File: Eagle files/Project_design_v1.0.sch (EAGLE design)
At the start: 4 parts

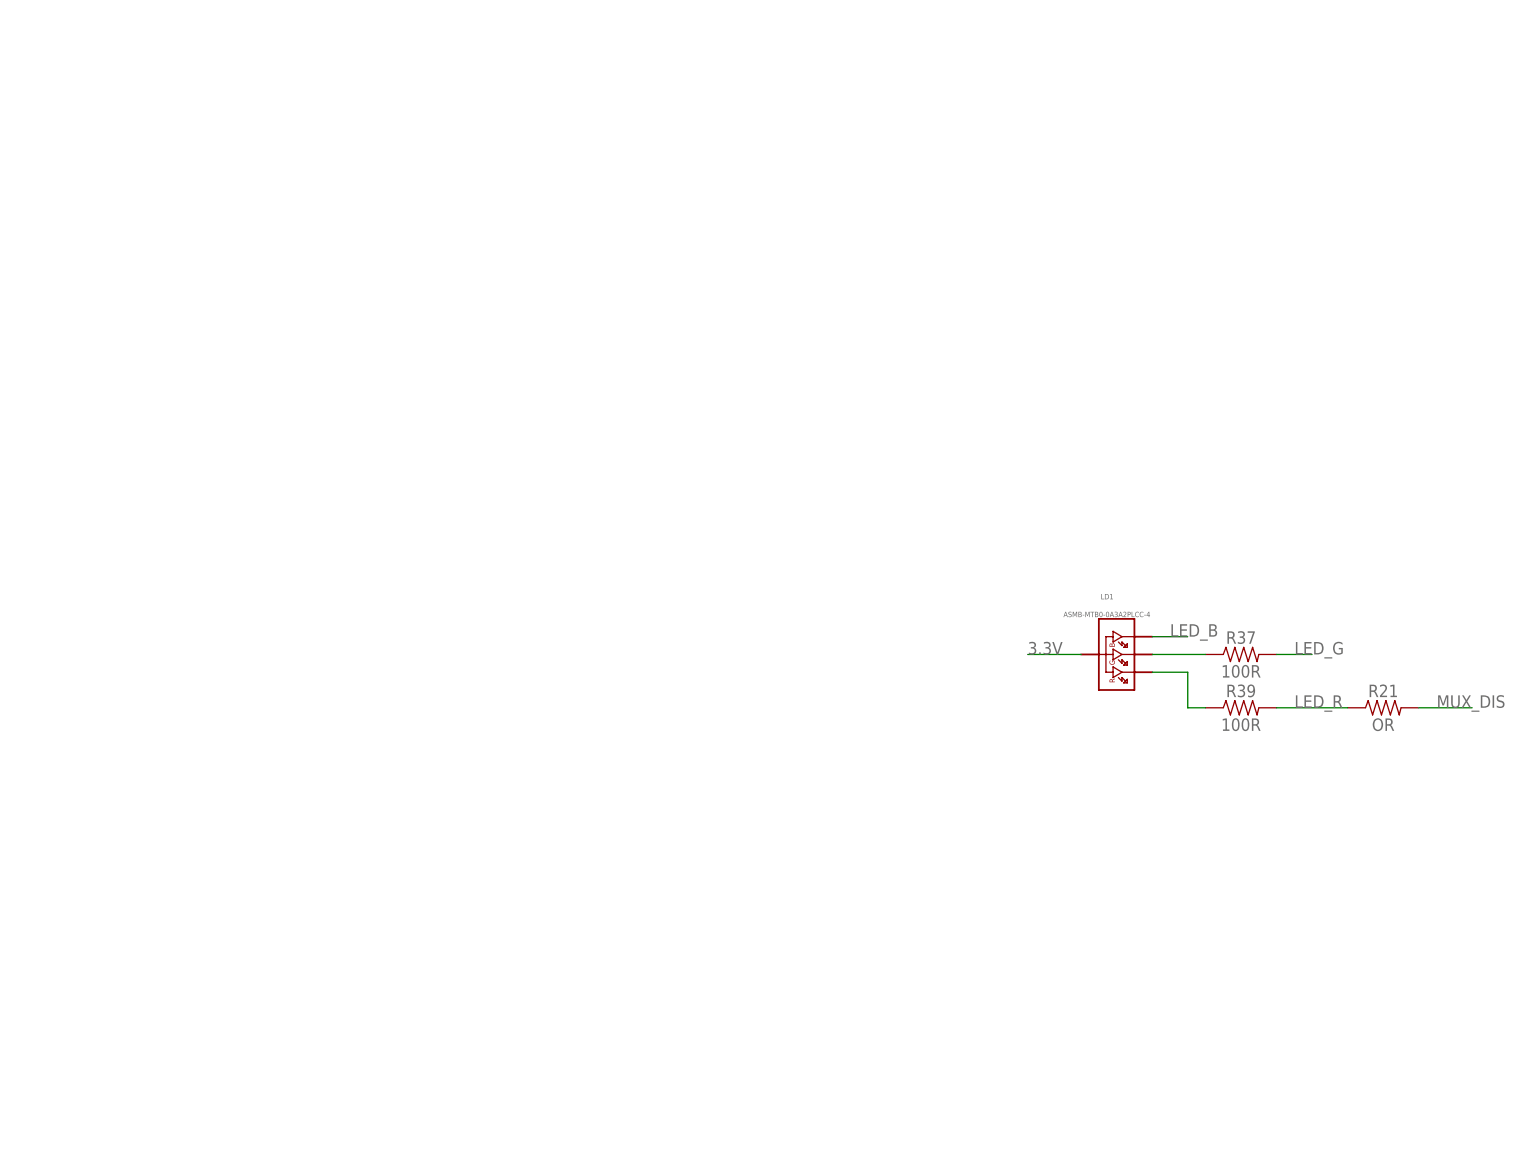
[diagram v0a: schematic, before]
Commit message: schematic des temperature, soil moisture, led, brightness sensor
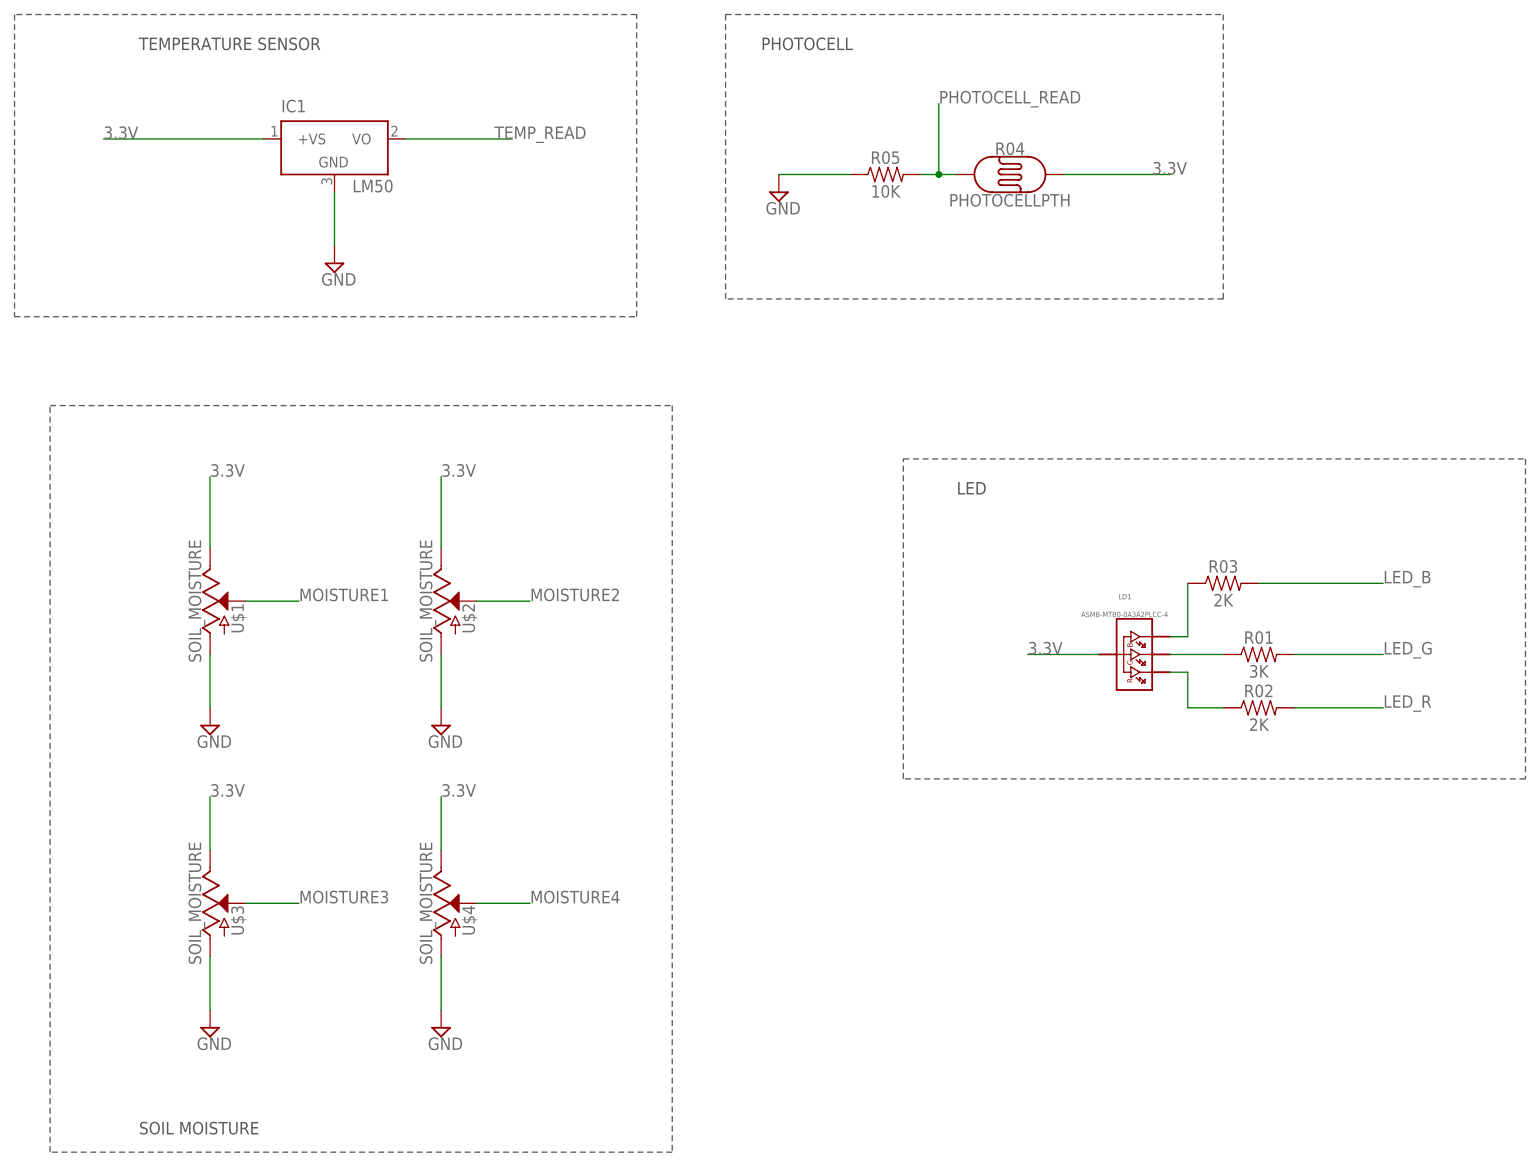
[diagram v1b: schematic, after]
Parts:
- removed R21: OR, custom_part:0603RESIST
- removed R37, R39: 100R, custom_part:0603RESIST
- added IC1: LM50, linear:LM50
- added R01: 3K, custom_part:0603RESIST
- added R02, R03: 2K, custom_part:0603RESIST
- added R04: PHOTOCELLPTH, SparkFun-Sensors:PHOTOCELLPTH
- added R05: 10K, custom_part:0603RESIST
- added U$1, U$2, U$3, U$4: SOIL_MOISTURE, potentiometer:SOIL_MOISTURE
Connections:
- removed net MUX_DIS: R21.2
- new net GND: R05.1, U$1.GND, U$2.GND, U$3.GND, U$4.GND
- new net MOISTURE1: U$1.VOUT
- new net MOISTURE2: U$2.VOUT
- new net MOISTURE3: U$3.VOUT
- new net MOISTURE4: U$4.VOUT
- new net N$1: LD1.2, R03.1
- new net N$4: IC1.GND
- new net PHOTOCELL_READ: R04.P$1, R05.2
- new net TEMP_READ: IC1.VO
- net 3.3V: now also IC1.+VS, R04.P$2, U$1.VCC, U$2.VCC, U$3.VCC, U$4.VCC
- net LED_B: now also R03.2; no longer LD1.2
- net LED_G: now also R01.2; no longer R37.2
- net LED_R: now also R02.2; no longer R21.1, R39.2
- net N$34: now also R01.1; no longer R37.1
- net N$35: now also R02.1; no longer R39.1
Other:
- note added: "LED"
- note added: "PHOTOCELL"
- note added: "SOIL MOISTURE"
- note added: "TEMPERATURE SENSOR"
- moved on the sheet: LD1

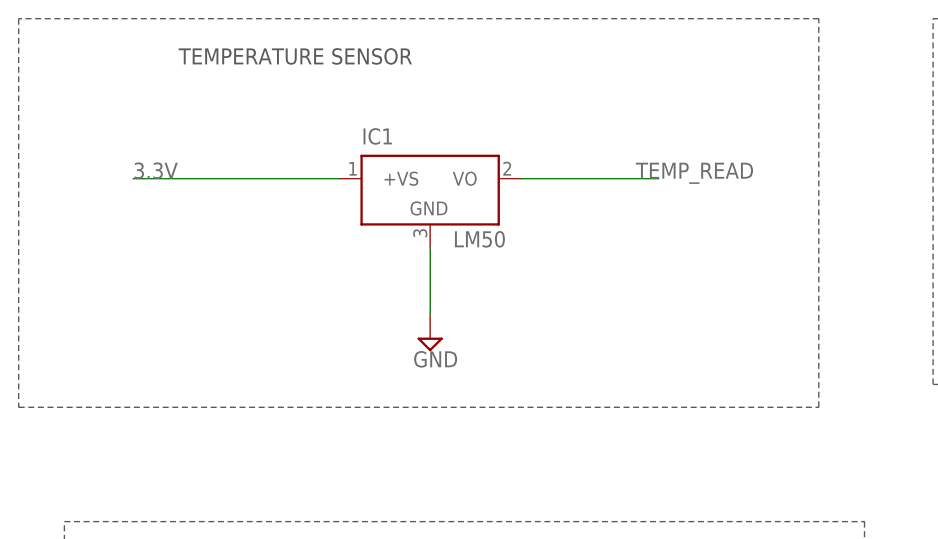
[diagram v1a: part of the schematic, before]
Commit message: temperature sensor schmetatic & packages edited
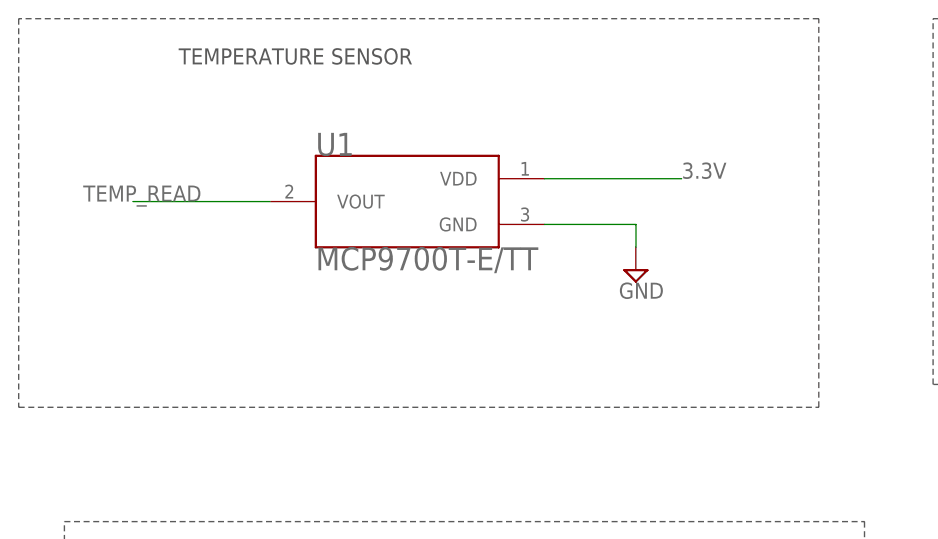
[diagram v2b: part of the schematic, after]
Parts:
- removed IC1: LM50, linear:LM50
- added U1: MCP9700T-E/TT, MCP9700T-E_TT:MCP9700T-E/TT
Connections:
- removed net N$4: IC1.GND
- net 3.3V: now also U1.VDD; no longer IC1.+VS
- net GND: now also U1.GND
- net TEMP_READ: now also U1.VOUT; no longer IC1.VO
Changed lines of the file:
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@@
 <setting verticaltext="up"/>
 </settings>
-<grid distance="0.1" unitdist="inch" unit="mm" style="lines" multiple="1" display="no" altdistance="0.01" altunitdist="inch" altunit="mm"/>
+<grid distance="0.1" unitdist="inch" unit="inch" style="lines" multiple="1" display="no" altdistance="0.01" altunitdist="inch" altunit="inch"/>
 <layers>
 <layer number="1" name="Top" color="4" fill="1" visible="no" active="no"/>
@@
 </part>
 <part name="SUPPLY1" library="supply2" library_urn="urn:adsk.eagle:library:372" deviceset="GND" device=""/>
-<part name="IC1" library="linear" library_urn="urn:adsk.eagle:library:262" deviceset="LM50" device="" package3d_urn="urn:adsk.eagle:package:16489/2"/>
 <part name="SUPPLY2" library="supply2" library_urn="urn:adsk.eagle:library:372" deviceset="GND" device=""/>
 <part name="U$1" library="potentiometer" deviceset="SOIL_MOISTURE" device=""/>
@@
 <part name="U$4" library="potentiometer" deviceset="SOIL_MOISTURE" device=""/>
 <part name="SUPPLY6" library="supply2" library_urn="urn:adsk.eagle:library:372" deviceset="GND" device=""/>
+<part name="U1" library="MCP9700T-E_TT" deviceset="MCP9700T-E/TT" device=""/>
 </parts>
 <sheets>
@@
 </instance>
 <instance part="SUPPLY1" gate="GND" x="30.48" y="132.08"/>
-<instance part="IC1" gate="G$1" x="-33.02" y="139.7"/>
-<instance part="SUPPLY2" gate="GND" x="-33.02" y="121.92"/>
+<instance part="SUPPLY2" gate="GND" x="-10.16" y="129.54"/>
 <instance part="U$1" gate="G$1" x="-50.8" y="73.66"/>
 <instance part="SUPPLY3" gate="GND" x="-50.8" y="55.88"/>
@@
 <instance part="U$4" gate="G$1" x="-17.78" y="30.48"/>
 <instance part="SUPPLY6" gate="GND" x="-17.78" y="12.7"/>
+<instance part="U1" gate="G$1" x="-35.56" y="137.16"/>
 </instances>
 <busses>
@@
 </segment>
 <segment>
-<pinref part="IC1" gate="G$1" pin="+VS"/>
-<wire x1="-43.18" y1="139.7" x2="-66.04" y2="139.7" width="0.1524" layer="91"/>
-<label x="-66.04" y="139.7" size="1.778" layer="95"/>
-</segment>
-<segment>
 <pinref part="U$1" gate="G$1" pin="VCC"/>
 <wire x1="-50.8" y1="81.28" x2="-50.8" y2="91.44" width="0.1524" layer="91"/>
@@
 <wire x1="-17.78" y1="38.1" x2="-17.78" y2="45.72" width="0.1524" layer="91"/>
 <label x="-17.78" y="45.72" size="1.778" layer="95"/>
+</segment>
+<segment>
+<pinref part="U1" gate="G$1" pin="VDD"/>
+<wire x1="-20.32" y1="139.7" x2="-5.08" y2="139.7" width="0.1524" layer="91"/>
+<label x="-5.08" y="139.7" size="1.778" layer="95"/>
 </segment>
 </net>
@@
 <wire x1="-17.78" y1="22.86" x2="-17.78" y2="15.24" width="0.1524" layer="91"/>
 </segment>
+<segment>
+<pinref part="U1" gate="G$1" pin="GND"/>
+<wire x1="-20.32" y1="134.62" x2="-10.16" y2="134.62" width="0.1524" layer="91"/>
+<pinref part="SUPPLY2" gate="GND" pin="GND"/>
+<wire x1="-10.16" y1="134.62" x2="-10.16" y2="132.08" width="0.1524" layer="91"/>
+</segment>
 </net>
 <net name="TEMP_READ" class="0">
 <segment>
-<pinref part="IC1" gate="G$1" pin="VO"/>
-<wire x1="-22.86" y1="139.7" x2="-7.62" y2="139.7" width="0.1524" layer="91"/>
-<label x="-10.16" y="139.7" size="1.778" layer="95"/>
-</segment>
-</net>
-<net name="N$4" class="0">
-<segment>
-<pinref part="IC1" gate="G$1" pin="GND"/>
-<wire x1="-33.02" y1="132.08" x2="-33.02" y2="124.46" width="0.1524" layer="91"/>
-</segment>
-</net>
+<wire x1="-66.04" y1="137.16" x2="-50.8" y2="137.16" width="0.1524" layer="91"/>
+<label x="-58.42" y="137.16" size="1.778" layer="95" rot="MR0"/>
+<pinref part="U1" gate="G$1" pin="VOUT"/>
+</segment>
+</net>
